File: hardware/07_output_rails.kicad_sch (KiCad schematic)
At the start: 6 parts, among them J7 Manual IDC wire landing

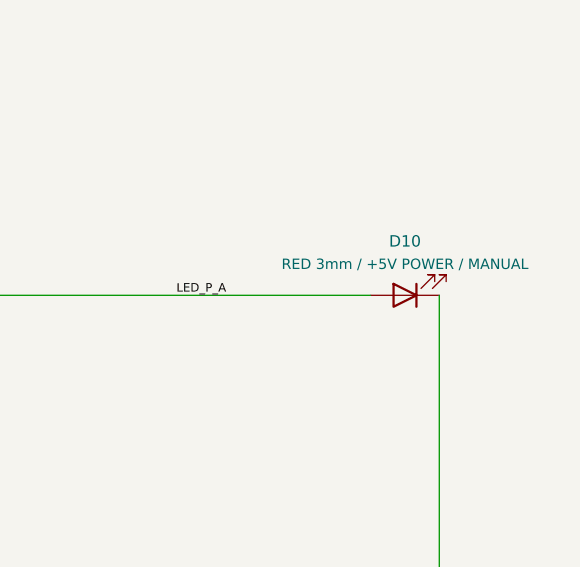
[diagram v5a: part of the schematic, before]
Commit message: Use standard vias and front-only Economy assembly with Basic passive networks and DNP LED
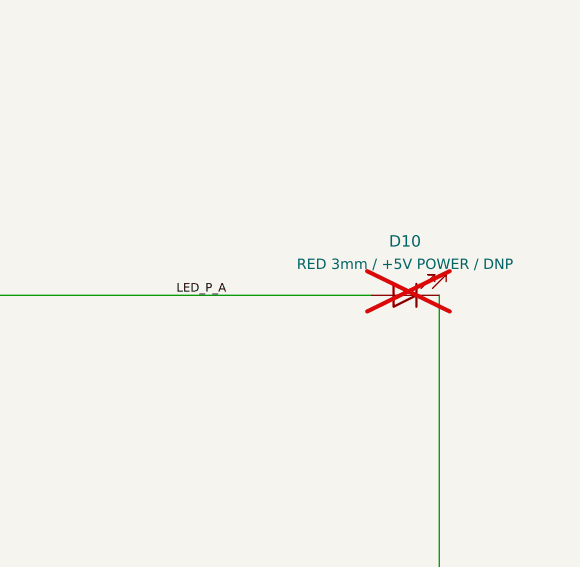
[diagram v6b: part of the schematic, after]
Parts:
- D10: value RED 3mm / +5V POWER / MANUAL -> RED 3mm / +5V POWER / DNP; JLCPCB Audit Requirements {"assembly": "manual", "reason": "User-selected manual inte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 -> {"reason": "D10 is DNP by user; no fitted purchasing or ass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; NOTE Single hand-soldered red3mm power LED: P5 -> R32 1k -> anod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 -> DNP by user: not purchased or fitted. Retain physical footp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; now not fitted
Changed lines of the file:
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@@
 		)
 	)
-	(symbol
-		(lib_id "BigModular:Device_LED")
-		(at 314.96 88.9 180)
-		(unit 1)
-		(body_style 1)
-		(exclude_from_sim no)
-		(in_bom yes)
-		(on_board yes)
-		(in_pos_files yes)
-		(dnp no)
-		(property "Reference" "D10"
-			(at 314.96 82.9 0)
-			(show_name no)
-			(do_not_autoplace no)
-			(effects
-				(font
-					(size 1.27 1.27)
-				)
-			)
-		)
-		(property "Value" "RED 3mm / +5V POWER / MANUAL"
-			(at 314.96 85.44 0)
-			(show_name no)
-			(do_not_autoplace no)
-			(effects
-				(font
-					(size 1.15 1.15)
-				)
-			)
-		)
-		(property "Footprint" "BigModular:LED_D3.0mm_Horizontal_O1.27mm_Z2.0mm_Edge"
-			(at 314.96 88.9 0)
-			(hide yes)
-			(show_name no)
-			(do_not_autoplace no)
-			(effects
-				(font
-					(size 1 1)
-				)
-			)
-		)
-		(property "Datasheet" ""
-			(at 314.96 88.9 0)
-			(hide yes)
-			(show_name no)
-			(do_not_autoplace no)
-			(effects
-				(font
-					(size 1 1)
-				)
-			)
-		)
-		(property "Description" ""
-			(at 314.96 88.9 0)
-			(show_name no)
-			(do_not_autoplace no)
-			(effects
-				(font
-					(size 1.27 1.27)
-				)
-			)
-		)
-		(property "MPN" ""
-			(at 314.96 88.9 0)
-			(hide yes)
-			(show_name no)
-			(do_not_autoplace no)
-			(effects
-				(font
-					(size 1 1)
-				)
-			)
-		)
-		(property "LCSC" ""
-			(at 314.96 88.9 0)
-			(hide yes)
-			(show_name no)
-			(do_not_autoplace no)
-			(effects
-				(font
-					(size 1 1)
-				)
-			)
-		)
-		(property "NOTE" "Single hand-soldered red3mm power LED: P5 -> R32 1k -> anode2; cathode1 GND. No automatic blink, no external control, not proof all rails are healthy. Top-cluster D10 hole/formed-lead envelope; exact MPN pending."
-			(at 314.96 88.9 0)
-			(hide yes)
-			(show_name no)
-			(do_not_autoplace no)
-			(effects
-				(font
-					(size 1 1)
-				)
-			)
-		)
-		(property "JLCPCB Exclude" "yes"
-			(at 314.96 88.9 0)
-			(hide yes)
-			(show_name no)
-			(do_not_autoplace no)
-			(effects
-				(font
-					(size 1 1)
-				)
-			)
-		)
-		(property "JLCPCB Audit Requirements" "{\"assembly\": \"manual\", \"reason\": \"User-selected manual interface/LED, excluded from JLC placement.\"}"
-			(at 314.96 88.9 0)
-			(hide yes)
-			(show_name no)
-			(do_not_autoplace no)
-			(effects
-				(font
-					(size 1 1)
-				)
-			)
-		)
-		(pin "1"
-		)
-		(pin "2"
-		)
-		(instances
-			(project "big_modular"
-				(path "/d567704c-57ad-5df1-b183-cadb01fd8972/a8d4c238-ef1c-5c41-9eba-d79c1c1014c4"
-					(reference "D10")
-					(unit 1)
-				)
-			)
-		)
-	)
+	(symbol (lib_id "BigModular:Device_LED") (at 314.96 88.9 180) (unit 1) (body_style 1) (exclude_from_sim no) (in_bom yes) (on_board yes) (in_pos_files yes) (dnp yes) (property "Reference" "D10" (at 314.96 82.9 0) (show_name no) (do_not_autoplace no) (effects (font (size 1.27 1.27)))) (property "Value" "RED 3mm / +5V POWER / DNP" (at 314.96 85.44 0) (show_name no) (do_not_autoplace no) (effects (font (size 1.15 1.15)))) (property "Footprint" "BigModular:LED_D3.0mm_Horizontal_O1.27mm_Z2.0mm_Edge" (at 314.96 88.9 0) (hide yes) (show_name no) (do_not_autoplace no) (effects (font (size 1 1)))) (property "Datasheet" "" (at 314.96 88.9 0) (hide yes) (show_name no) (do_not_autoplace no) (effects (font (size 1 1)))) (property "Description" "" (at 314.96 88.9 0) (show_name no) (do_not_autoplace no) (effects (font (size 1.27 1.27)))) (property "MPN" "" (at 314.96 88.9 0) (hide yes) (show_name no) (do_not_autoplace no) (effects (font (size 1 1)))) (property "LCSC" "" (at 314.96 88.9 0) (hide yes) (show_name no) (do_not_autoplace no) (effects (font (size 1 1)))) (property "NOTE" "DNP by user: not purchased or fitted. Retain physical footprint and indicator circuit: P5 -> R32 1k -> anode2; cathode1 GND. No automatic blink, no external control, not proof all rails are healthy. Top-cluster D10 hole/formed-lead envelope; no LED procurement requested." (at 314.96 88.9 0) (hide yes) (show_name no) (do_not_autoplace no) (effects (font (size 1 1)))) (property "JLCPCB Exclude" "yes" (at 314.96 88.9 0) (hide yes) (show_name no) (do_not_autoplace no) (effects (font (size 1 1)))) (property "JLCPCB Audit Requirements" "{\"reason\": \"D10 is DNP by user; no fitted purchasing or assembly.\"}" (at 314.96 88.9 0) (hide yes) (show_name no) (do_not_autoplace no) (effects (font (size 1 1)))) (pin "1") (pin "2") (instances (project "big_modular" (path "/d567704c-57ad-5df1-b183-cadb01fd8972/a8d4c238-ef1c-5c41-9eba-d79c1c1014c4" (reference "D10") (unit 1)))))
  (wire (pts (xy 83.82 107.95) (xy 85.09 107.95)) (stroke (width 0) (type default))) (wire (pts (xy 85.09 107.95) (xy 85.09 109.22)) (stroke (width 0) (type default))) (wire (pts (xy 83.82 109.22) (xy 85.09 109.22)) (stroke (width 0) (type default))) (junction (at 85.09 109.22) (diameter 0) (color 0 0 0 0)) (wire (pts (xy 142.24 107.95) (xy 143.51 107.95)) (stroke (width 0) (type default))) (wire (pts (xy 143.51 107.95) (xy 143.51 109.22)) (stroke (width 0) (type default))) (wire (pts (xy 142.24 109.22) (xy 143.51 109.22)) (stroke (width 0) (type default))) (junction (at 143.51 109.22) (diameter 0) (color 0 0 0 0)))
